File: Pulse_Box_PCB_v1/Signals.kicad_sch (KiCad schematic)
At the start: 22 parts, among them J2 Conn_02x05_Odd_Even, J3 USB_B_Micro, J4 Conn_01x03_Pin, U1 STM32F407VGTx, U2 SN74LV1T34DBV, Y1 8MHz Crystal

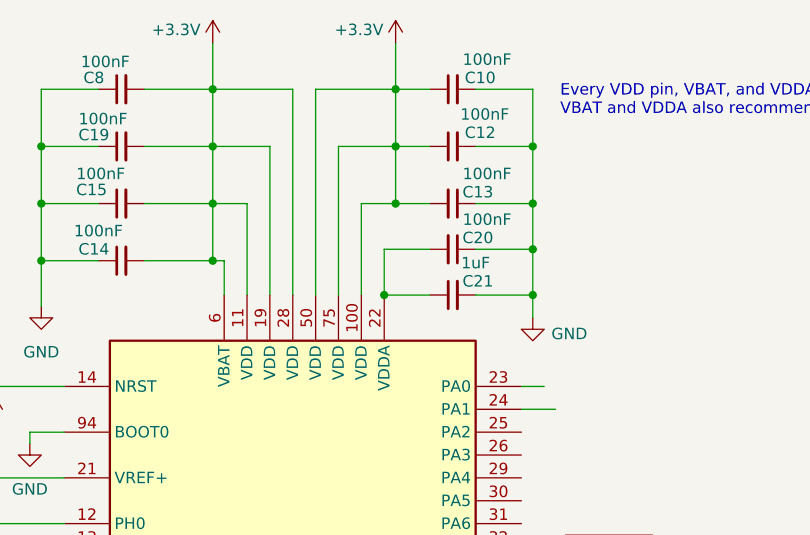
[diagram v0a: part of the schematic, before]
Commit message: add v2 board design with esp32-s3 wroom module, moved versions into dedicated directories
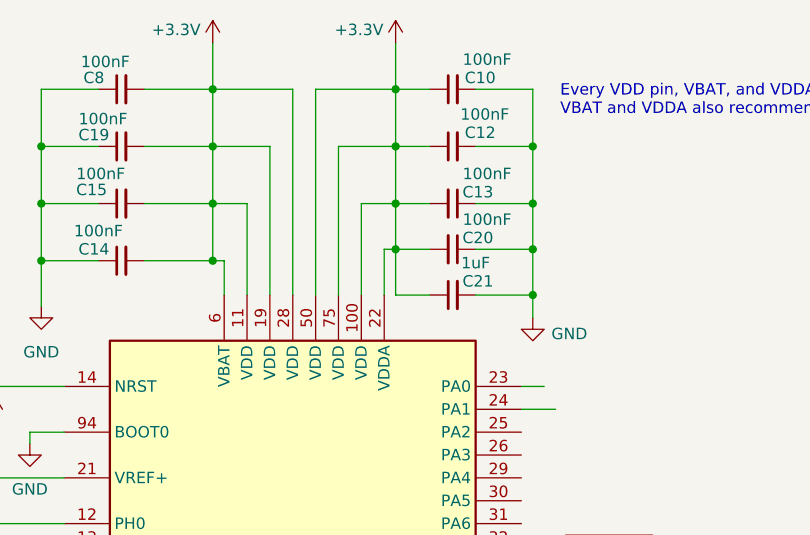
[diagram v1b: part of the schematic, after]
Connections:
- net +3.3V: now also C20.2, C21.1, U1.22 (VDDA)
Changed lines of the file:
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@@
+	)
+	(junction
+		(at 86.36 38.1)
+		(diameter 0)
+		(color 0 0 0 0)
 	)
 	(junction
@@
 	)
 	(junction
-		(at 85.09 43.18)
-		(diameter 0)
-		(color 0 0 0 0)
-	)
-	(junction
 		(at 172.72 82.55)
 		(diameter 0)
@@
 	(wire
 		(pts
+			(xy 86.36 38.1) (xy 90.17 38.1)
+		)
+		(stroke
+			(width 0)
+			(type default)
+		)
+	)
+	(wire
+		(pts
 			(xy 255.27 138.43) (xy 255.27 142.24)
 		)
@@
 	(wire
 		(pts
+			(xy 90.17 43.18) (xy 86.36 43.18)
+		)
+		(stroke
+			(width 0)
+			(type default)
+		)
+	)
+	(wire
+		(pts
 			(xy 77.47 187.96) (xy 77.47 190.5)
 		)
@@
 	(wire
 		(pts
+			(xy 85.09 38.1) (xy 85.09 43.18)
+		)
+		(stroke
+			(width 0)
+			(type default)
+		)
+	)
+	(wire
+		(pts
 			(xy 215.9 138.43) (xy 222.25 138.43)
 		)
@@
 	(wire
 		(pts
+			(xy 86.36 38.1) (xy 86.36 33.02)
+		)
+		(stroke
+			(width 0)
+			(type default)
+		)
+	)
+	(wire
+		(pts
 			(xy 95.25 20.32) (xy 101.6 20.32)
 		)
@@
 	(wire
 		(pts
-			(xy 85.09 43.18) (xy 90.17 43.18)
-		)
-		(stroke
-			(width 0)
-			(type default)
-		)
-	)
-	(wire
-		(pts
 			(xy 49.53 68.58) (xy 38.1 68.58)
 		)
@@
 	(wire
 		(pts
+			(xy 85.09 38.1) (xy 86.36 38.1)
+		)
+		(stroke
+			(width 0)
+			(type default)
+		)
+	)
+	(wire
+		(pts
 			(xy 46.99 39.37) (xy 46.99 44.45)
 		)
@@
 	(wire
 		(pts
-			(xy 85.09 38.1) (xy 90.17 38.1)
-		)
-		(stroke
-			(width 0)
-			(type default)
-		)
-	)
-	(wire
-		(pts
 			(xy 86.36 20.32) (xy 90.17 20.32)
 		)
@@
 	(wire
 		(pts
+			(xy 86.36 43.18) (xy 86.36 38.1)
+		)
+		(stroke
+			(width 0)
+			(type default)
+		)
+	)
+	(wire
+		(pts
 			(xy 139.7 127) (xy 156.21 127)
 		)
 		(stroke
-			(width 0)
-			(type default)
-		)
-	)
-	(wire
-		(pts
-			(xy 85.09 43.18) (xy 85.09 38.1)
-		)
-		(stroke
